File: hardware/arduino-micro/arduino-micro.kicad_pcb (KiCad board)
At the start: 2 copper layers, 80 x 44.5 mm, 15 parts, among them J1 PJ-028-SMT-TR, M1 Fan_4pin, SW1 Rotary_Encoder, U1 TM1637, U2 CA56-12CGKWA

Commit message: hardware updates: fix input voltage, cnc tweaks (#2)
* Ch ch ch changes.

* update for latest kicad
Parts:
- added R6: 27k, coddingtonbear:0805_Milling, F.Cu at (204.2, 146.2)
- added R7: 10k, coddingtonbear:0805_Milling, F.Cu at (204.2, 148.0)
- C1: footprint Capacitor_THT:CP_Radial_Tantal_D4.5mm_P2.50mm -> Capacitors_THT:CP_Radial_D6.3mm_P2.50mm
- C2, C3, C4: footprint Capacitor_SMD:C_0805_2012Metric -> coddingtonbear:0805_Milling
- R1, R2, R3, R4, R5: footprint Resistor_SMD:R_0805_2012Metric -> coddingtonbear:0805_Milling
- moved R5 3.94 mm to (222.4, 117.0)
- moved C4 3.66 mm to (224.6, 117.0)
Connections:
- XA1 pad D12: /7S_CLK -> Net-(XA1-PadD12)
- XA1 pad D13: /7S_IO -> Net-(XA1-PadD13)
- XA1 pad D7: Net-(M1-Pad3) -> Net-(R6-Pad1)
- XA1 pad MOSI: Net-(XA1-PadMOSI) -> /7S_IO
- XA1 pad SCK: Net-(XA1-PadSCK) -> /7S_CLK
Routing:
- net /7S_IO: track 34.1 -> 88.1 mm, vias 1 -> 3
- net /7S_CLK: track 48.6 -> 88.1 mm
- net GND: track 137.9 -> 173.1 mm, vias 3 -> 4
- net Net-(U1-Pad3): track 21.7 -> 34.4 mm
- net Net-(R6-Pad1): track 0.00 -> 8.20 mm, vias 0 -> 1
- net Net-(U1-Pad8): track 24.1 -> 31.3 mm
- net Net-(U1-Pad12): track 22.3 -> 27.0 mm
- net Net-(U1-Pad9): track 42.4 -> 46.9 mm
- net Net-(U1-Pad2): track 41.5 -> 45.2 mm
- net /5V: track 116.4 -> 118.3 mm
- net Net-(U1-Pad7): track 15.4 -> 17.2 mm
- net Net-(U1-Pad14): track 29.5 -> 31.2 mm
- net Net-(U1-Pad4): track 12.9 -> 14.2 mm
- net Net-(M1-Pad3): track 45.9 -> 45.2 mm, vias 1 -> 0
- net +12V: track 32.2 -> 32.9 mm
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
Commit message: checkpoint before removing board
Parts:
- C1: footprint Capacitors_THT:CP_Radial_D6.3mm_P2.50mm -> Capacitor_Tantalum_SMD:CP_EIA-7343-15_Kemet-W
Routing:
- net /5V: track 118.3 -> 124.1 mm

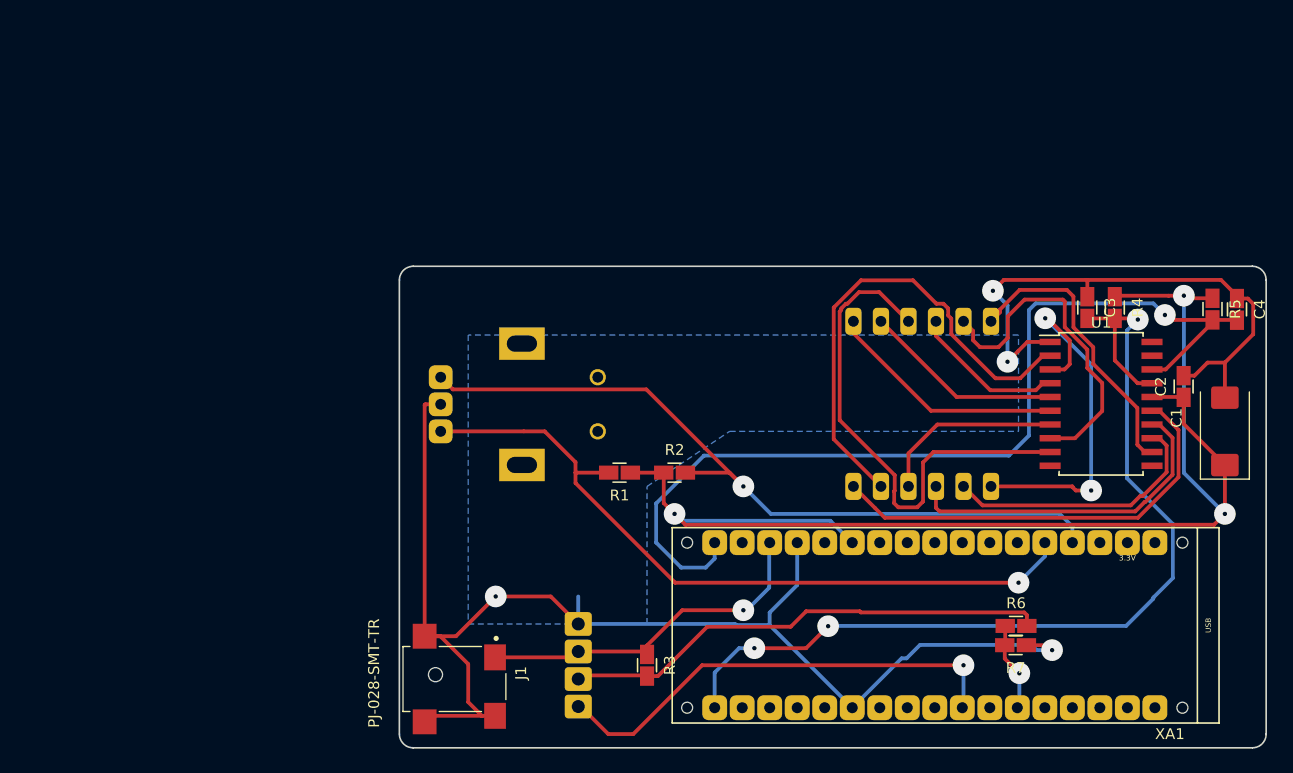
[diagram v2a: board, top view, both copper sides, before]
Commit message: redesign board, additional buttons/i2c header
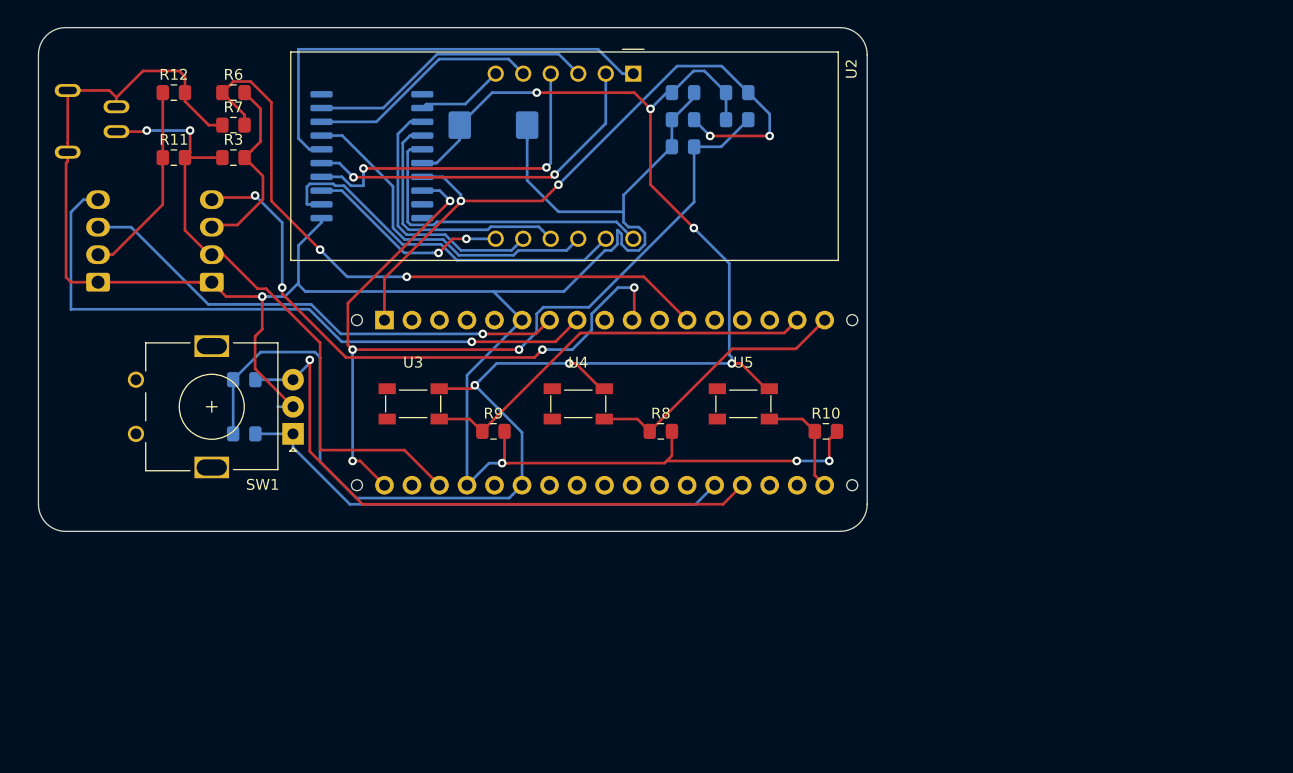
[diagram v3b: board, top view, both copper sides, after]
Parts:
- added J2: i2c_header, Connector_Molex:Molex_KK-254_AE-6410-04A_1x04_P2.54mm_Vertical, B.Cu at (119.5, 114.5)
- added R10: 10k, Resistor_SMD:R_0805_2012Metric_Pad1.15x1.40mm_HandSolder, F.Cu at (186.7, 128.3)
- added R11: 14k, Resistor_SMD:R_0805_2012Metric_Pad1.15x1.40mm_HandSolder, F.Cu at (126.5, 103.0)
- added R12: 10k, Resistor_SMD:R_0805_2012Metric_Pad1.15x1.40mm_HandSolder, F.Cu at (126.5, 97.0)
- added R8: 10k, Resistor_SMD:R_0805_2012Metric_Pad1.15x1.40mm_HandSolder, F.Cu at (171.4, 128.3)
- added R9: 10k, Resistor_SMD:R_0805_2012Metric_Pad1.15x1.40mm_HandSolder, F.Cu at (156.0, 128.3)
- added U3: BUTTON_1, squeeze-misc:PTS525_SM15_SMTR2_LFS, F.Cu at (148.6, 125.7)
- added U4: BUTTON_2, squeeze-misc:PTS525_SM15_SMTR2_LFS, F.Cu at (163.8, 125.7)
- added U5: BUTTON_3, squeeze-misc:PTS525_SM15_SMTR2_LFS, F.Cu at (179.1, 125.7)
- C1: footprint Capacitor_Tantalum_SMD:CP_EIA-7343-15_Kemet-W -> Capacitor_Tantalum_SMD:CP_EIA-7343-31_Kemet-D; moved to B.Cu
- C2, C3, C4, R1, R2, R4, R5: footprint coddingtonbear:0805_Milling -> Resistor_SMD:R_0805_2012Metric_Pad1.15x1.40mm_HandSolder; moved to B.Cu
- J1: value PJ-028-SMT-TR -> PJ-088CH; footprint PJ-028-SMT-TR:CUI_PJ-028-SMT-TR -> PJ-088CH:CUI_PJ-088CH; moved to B.Cu
- R3, R6, R7: footprint coddingtonbear:0805_Milling -> Resistor_SMD:R_0805_2012Metric_Pad1.15x1.40mm_HandSolder
- SW1, U2: moved to F.Cu
- U1, XA1: moved to B.Cu
- moved R6 87.4 mm to (132.0, 97.0)
- moved R7 86.7 mm to (132.0, 100.0), turned to 0 degrees
- moved C1 73.2 mm to (156.0, 100.0), turned to 0 degrees
- moved U1 71.1 mm to (144.8, 102.9)
- moved J1 63.9 mm to (114.0, 100.0), turned to 0 degrees
- moved R3 60.4 mm to (132.0, 103.0), turned to 0 degrees
- moved C2 53.6 mm to (173.5, 97.0), turned to 0 degrees
- moved C4 53.3 mm to (173.5, 102.0), turned to 0 degrees
- moved R5 47.2 mm to (178.5, 99.5), turned to 0 degrees
- moved M1 46.3 mm to (130.0, 114.5), turned to 90 degrees
- moved C3 41.2 mm to (173.5, 99.5), turned to 0 degrees
- moved R2 40.6 mm to (133.0, 123.5)
- moved R4 40.1 mm to (178.5, 97.0), turned to 0 degrees
- moved R1 34.8 mm to (133.0, 128.5), turned to 0 degrees
- moved U2 30.6 mm to (168.9, 95.2)
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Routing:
- net Net-(J2-Pad4): track 0.00 -> 60.7 mm, vias 0 -> 1
- net Net-(R6-Pad1): track 8.20 -> 61.6 mm, vias 1 -> 2
- net Net-(J2-Pad3): track 0.00 -> 46.3 mm, vias 0 -> 1
- net GND: track 173.0 -> 216.1 mm
- net Net-(R9-Pad1): track 0.00 -> 37.8 mm
- net /5V: track 124.1 -> 155.6 mm, vias 3 -> 6
- net Net-(M1-Pad3): track 45.2 -> 17.9 mm
- net +12V: track 32.9 -> 59.8 mm, vias 1 -> 2
- net Net-(R8-Pad1): track 0.00 -> 25.1 mm
- net /7S_IO: track 88.1 -> 63.9 mm, vias 3 -> 4
- net Net-(R1-Pad2): track 68.1 -> 46.5 mm, vias 1 -> 0
- net Net-(U1-Pad6): track 22.2 -> 42.6 mm
- net Net-(U1-Pad9): track 46.9 -> 26.5 mm
- net Net-(U1-Pad12): track 27.0 -> 8.10 mm
- net Net-(J2-Pad2): track 0.00 -> 18.2 mm
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- removed copper zone on B.Cu, net GND
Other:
- board size 80 x 44.5 mm -> 76.5 x 46.5 mm
- net class Default: trace_width 0.35 -> 0.25; via_dia 2 -> 0.8
- rule pad_to_mask_clearance: 0.051 -> 0.2032

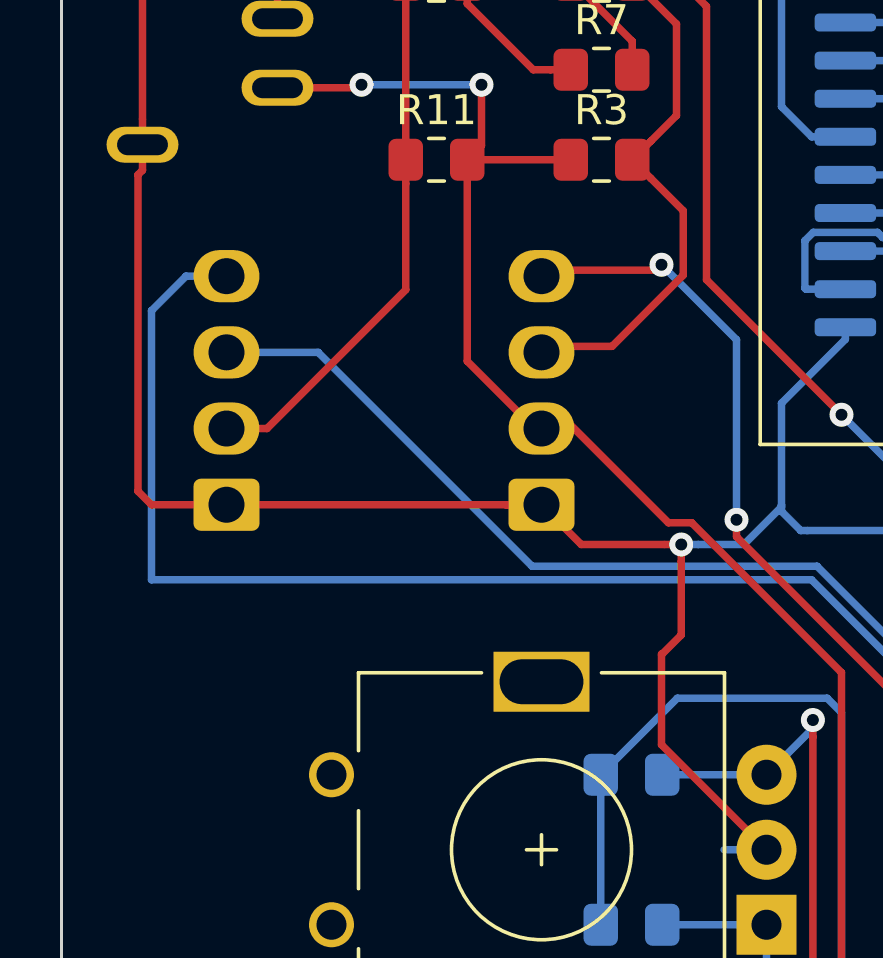
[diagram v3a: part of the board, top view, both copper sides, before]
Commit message: fix 5v for i2c header
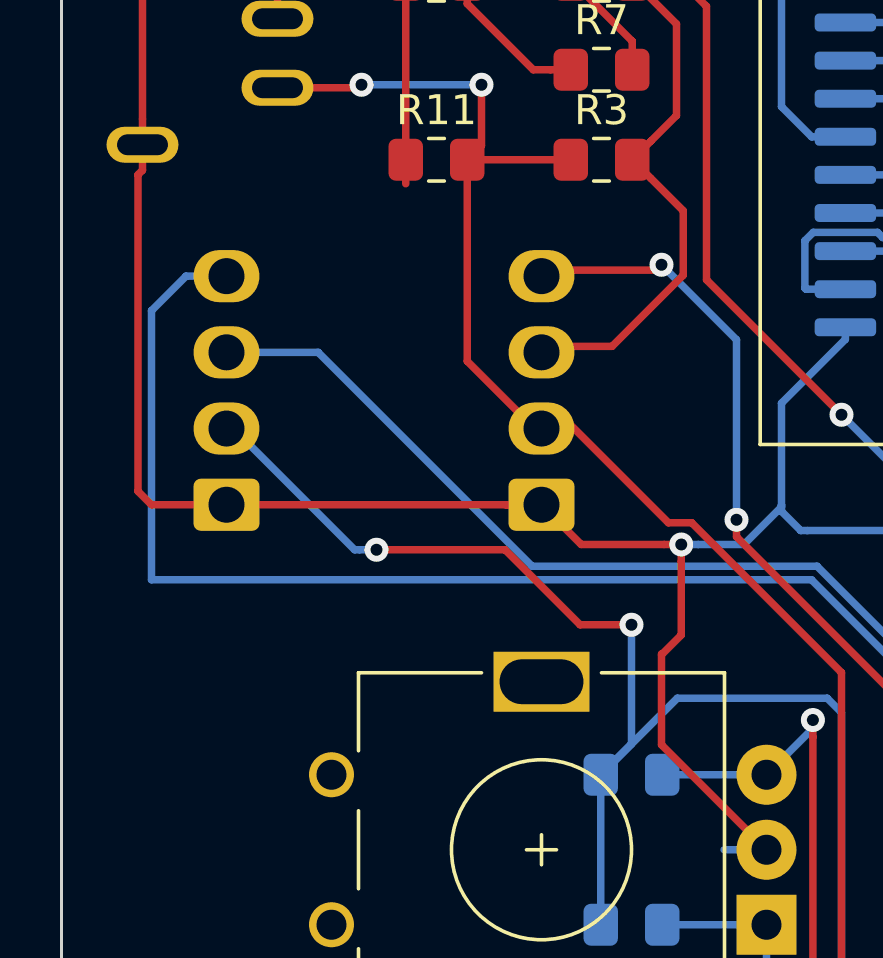
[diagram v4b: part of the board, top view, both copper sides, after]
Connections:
- J2 pad 2: Net-(J2-Pad2) -> /5V
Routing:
- net /5V: track 155.6 -> 177.3 mm, vias 6 -> 8
- net Net-(J2-Pad2): track 18.2 -> 6.80 mm
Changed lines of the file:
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@@
     (thickness 1.6)
     (drawings 8)
-    (tracks 404)
+    (tracks 412)
     (zones 0)
     (modules 26)
@@
       (net 54 "Net-(J2-Pad3)"))
     (pad 2 thru_hole oval (at 2.54 0 90) (size 1.74 2.2) (drill 1.2) (layers *.Cu *.Mask)
-      (net 55 "Net-(J2-Pad2)"))
+      (net 2 /5V))
     (pad 1 thru_hole roundrect (at 0 0 90) (size 1.74 2.2) (drill 1.2) (layers *.Cu *.Mask) (roundrect_rratio 0.143678)
       (net 1 GND))
@@
   (segment (start 157.776401 134.103599) (end 158.64 133.24) (width 0.25) (layer B.Cu) (net 2))
   (segment (start 131.975 123.5) (end 131.975 128.5) (width 0.25) (layer B.Cu) (net 2))
+  (via (at 124.5 116) (size 0.8) (drill 0.4) (layers F.Cu B.Cu) (net 2))
+  (via (at 133 118.5) (size 0.8) (drill 0.4) (layers F.Cu B.Cu) (net 2))
+  (segment (start 131.285002 118.5) (end 133 118.5) (width 0.25) (layer F.Cu) (net 2))
+  (segment (start 124.5 116) (end 128.785002 116) (width 0.25) (layer F.Cu) (net 2))
+  (segment (start 128.785002 116) (end 131.285002 118.5) (width 0.25) (layer F.Cu) (net 2))
+  (segment (start 133 122.475) (end 131.975 123.5) (width 0.25) (layer B.Cu) (net 2))
+  (segment (start 133 118.5) (end 133 122.475) (width 0.25) (layer B.Cu) (net 2))
+  (segment (start 123.934315 116) (end 124.5 116) (width 0.25) (layer B.Cu) (net 2))
+  (segment (start 123.77 116) (end 123.934315 116) (width 0.25) (layer B.Cu) (net 2))
+  (segment (start 119.73 111.96) (end 123.77 116) (width 0.25) (layer B.Cu) (net 2))
+  (segment (start 119.5 111.96) (end 119.73 111.96) (width 0.25) (layer B.Cu) (net 2))
   (via (at 153 107) (size 0.8) (drill 0.4) (layers F.Cu B.Cu) (net 3))
   (segment (start 150.555 104.775) (end 149.43 104.775) (width 0.25) (layer B.Cu) (net 3))
@@
   (segment (start 154.452213 119.27499) (end 155.017898 119.27499) (width 0.25) (layer B.Cu) (net 54))
   (segment (start 125.475 97) (end 125.475 103) (width 0.25) (layer F.Cu) (net 55))
-  (segment (start 120.85 111.96) (end 125.475 107.335) (width 0.25) (layer F.Cu) (net 55))
-  (segment (start 119.5 111.96) (end 120.85 111.96) (width 0.25) (layer F.Cu) (net 55))
-  (segment (start 125.475 107.335) (end 125.475 103.8) (width 0.25) (layer F.Cu) (net 55))
   (segment (start 125.475 103.8) (end 125.475 103) (width 0.25) (layer F.Cu) (net 55))
 )

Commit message: board updates for prototype
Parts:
- J1: value PJ-088CH -> PJ-083H; footprint PJ-088CH:CUI_PJ-088CH -> squeeze-misc:CUI_PJ-083H
- moved J1 2.83 mm to (112.0, 98.0)
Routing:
- net Net-(J1-PadS1): track 0.00 -> 10.3 mm
- net GND: track 216.1 -> 217.5 mm, vias 4 -> 5
- net Net-(J2-Pad2): track 6.80 -> 7.42 mm
- net +12V: track 59.8 -> 59.2 mm
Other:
- board size 76.5 x 46.5 mm -> 78 x 47 mm
